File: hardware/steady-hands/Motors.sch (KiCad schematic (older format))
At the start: 6 parts

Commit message: Adds new components
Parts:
- removed Q?: VND5N07-E, Package_TO_SOT_SMD:TO-252-2, symbol Device:Q_NMOS_GDS
- removed R?: 0, symbol Device:R
- added Q?: DMN2004WKQ, Package_TO_SOT_SMD:SOT-323_SC-70, symbol Transistor_FET:DMN2041L
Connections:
- wire segments 20 -> 19
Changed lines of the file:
@@
 $Descr A4 11693 8268
 encoding utf-8
-Sheet 4 6
+Sheet 4 7
 Title ""
 Date ""
@@
 	1    6950 3700
 	1    0    0    -1
-$EndComp
-$Comp
-L Device:Q_NMOS_GDS Q?
-U 1 1 5EF9AE62
-P 5300 3650
-F 0 "Q?" H 5504 3696 50  0000 L CNN
-F 1 "VND5N07-E" H 5504 3605 50  0000 L CNN
-F 2 "Package_TO_SOT_SMD:TO-252-2" H 5500 3750 50  0001 C CNN
-F 3 "~" H 5300 3650 50  0001 C CNN
-	1    5300 3650
-	1    0    0    -1
-$EndComp
-$Comp
-L Device:R R?
-U 1 1 5EF9AE68
-P 4700 3650
-F 0 "R?" V 4493 3650 50  0000 C CNN
-F 1 "0" V 4584 3650 50  0000 C CNN
-F 2 "" V 4630 3650 50  0001 C CNN
-F 3 "~" H 4700 3650 50  0001 C CNN
-	1    4700 3650
-	0    1    1    0
 $EndComp
 $Comp
@@
 	5100 3650 5000 3650
 Wire Wire Line
-	4550 3650 4400 3650
-Wire Wire Line
 	5000 3800 5000 3650
 Connection ~ 5000 3650
-Wire Wire Line
-	5000 3650 4850 3650
 Wire Wire Line
 	5400 3850 5400 4300
@@
 Text HLabel 4400 3650 0    50   Input ~ 0
 EN
+Wire Wire Line
+	4400 3650 5000 3650
+$Comp
+L Transistor_FET:DMN2041L Q?
+U 1 1 5EFAB5CE
+P 5300 3650
+F 0 "Q?" H 5504 3696 50  0000 L CNN
+F 1 "DMN2004WKQ" H 5504 3605 50  0000 L CNN
+F 2 "Package_TO_SOT_SMD:SOT-323_SC-70" H 5500 3575 50  0001 L CIN
+F 3 "https://www.mouser.com/datasheet/2/115/DMN2004WKQ-1019748.pdf" H 5300 3650 50  0001 L CNN
+	1    5300 3650
+	1    0    0    -1
+$EndComp
 $EndSCHEMATC

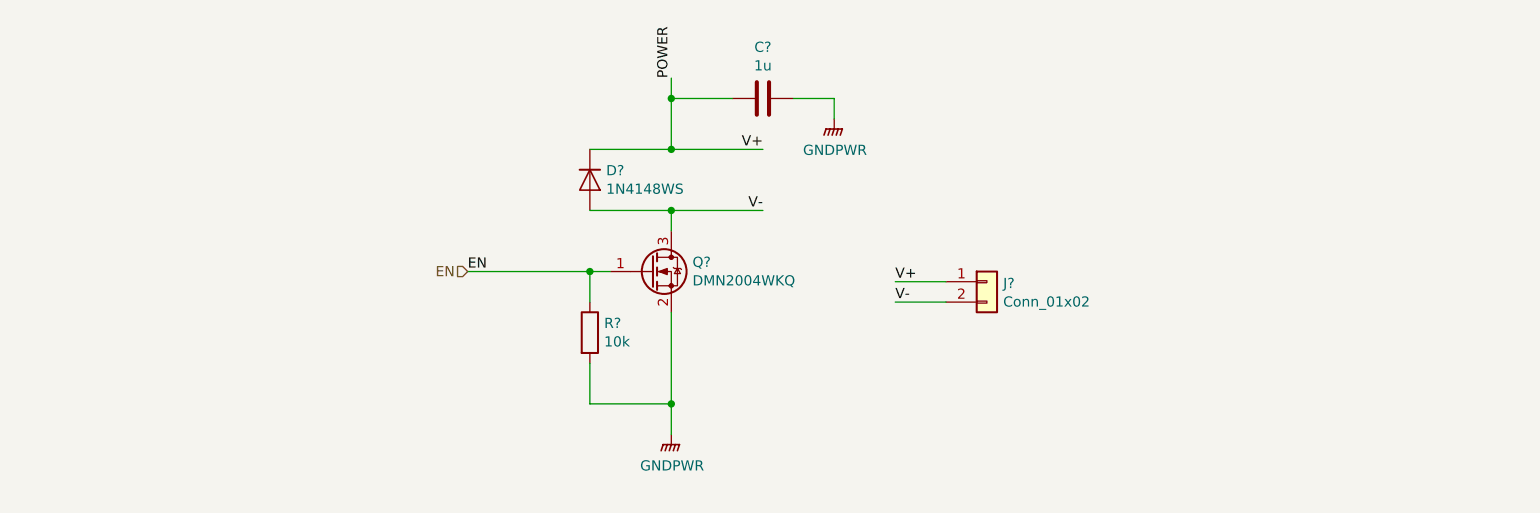
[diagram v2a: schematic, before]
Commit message: Adds second motor components
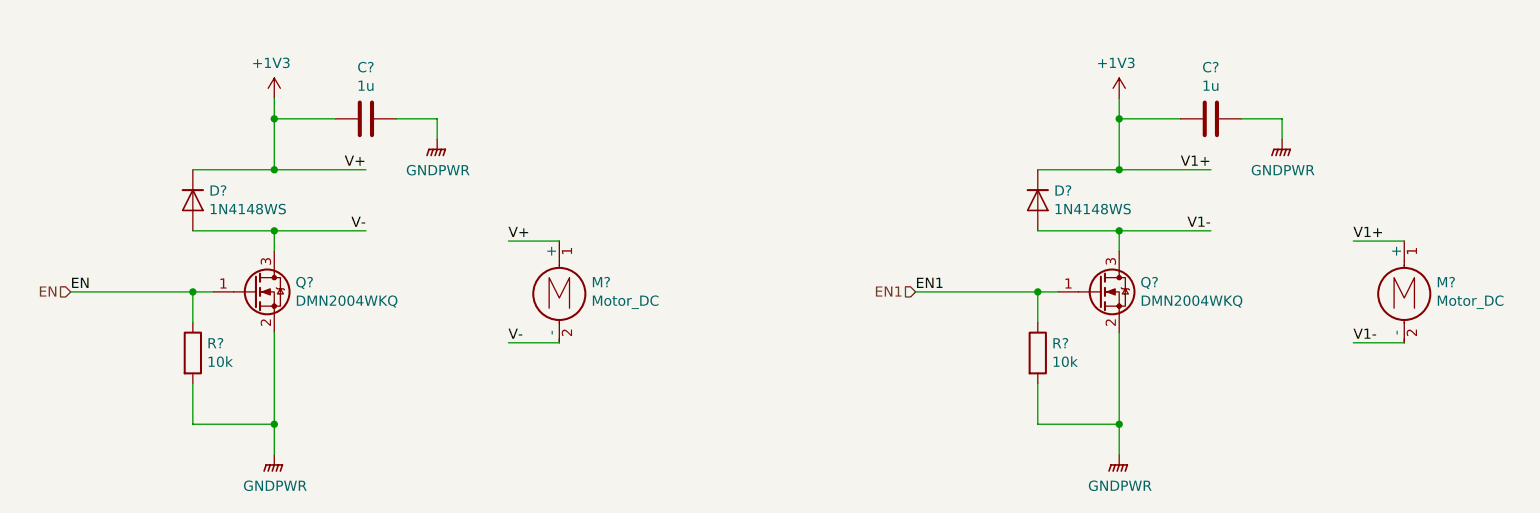
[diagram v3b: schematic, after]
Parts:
- removed J?: Conn_01x02, symbol Connector_Generic:Conn_01x02
- added C?: 1u, symbol Device:C
- added D?: 1N4148WS, Diode_SMD:D_SOD-323, symbol Diode:1N4148WS
- added M? (x2): Motor_DC, symbol Motor:Motor_DC
- added Q?: DMN2004WKQ, Package_TO_SOT_SMD:SOT-323_SC-70, symbol Transistor_FET:DMN2041L
- added R?: 10k, symbol Device:R
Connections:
- net GNDPWR: now also C?.1, Q?.2 (S), R?.2
- net V-: now also M?.2 (-)
- net POWER renamed +1V3
- net +1V3: now also C?.2, D?.1 (K), M?.1 (+), M?.1 (+)
- new net EN1: Q?.1 (G), R?.1
- new net V1-: D?.2 (A), M?.2 (-), Q?.3 (D)
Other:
- moved on the sheet: C?, D?, Q?, R?

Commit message: Completes schematic connections
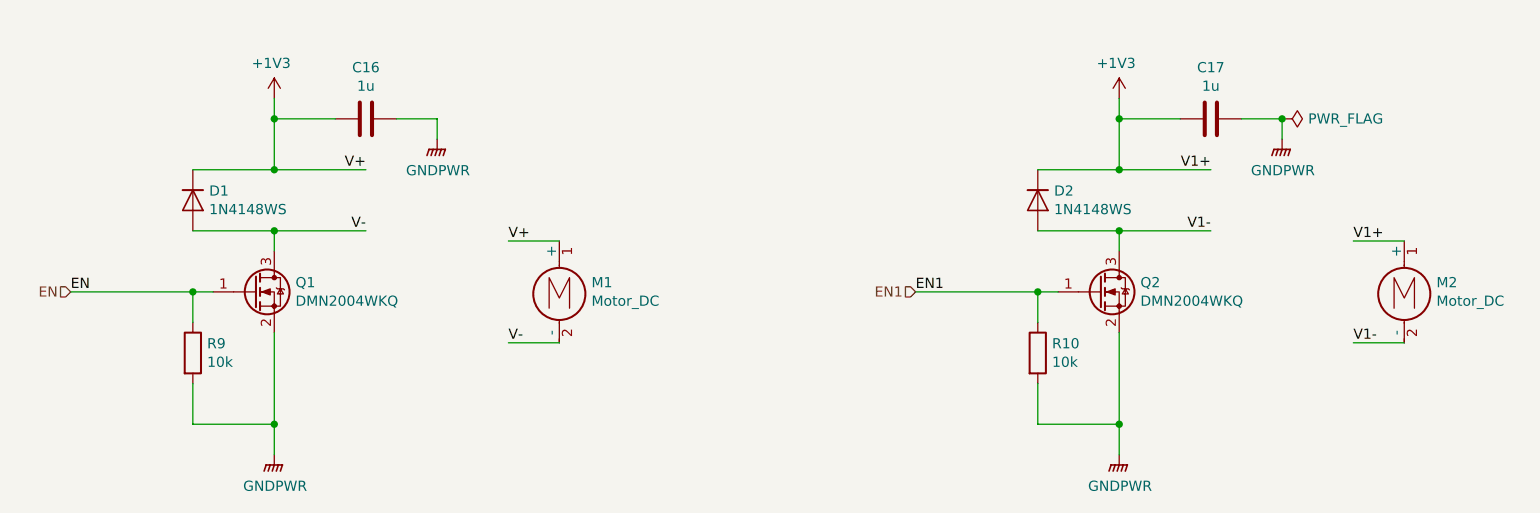
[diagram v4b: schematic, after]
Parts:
- gave numbers to parts that had none: 10
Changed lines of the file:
@@
 $Descr A4 11693 8268
 encoding utf-8
-Sheet 4 7
+Sheet 3 7
 Title ""
 Date ""
@@
 $EndDescr
 $Comp
-L Device:R R?
+L Device:R R9
 U 1 1 5EF9AE6E
 P 3050 4050
-F 0 "R?" H 3120 4096 50  0000 L CNN
+F 0 "R9" H 3120 4096 50  0000 L CNN
 F 1 "10k" H 3120 4005 50  0000 L CNN
 F 2 "" V 2980 4050 50  0001 C CNN
@@
 $EndComp
 $Comp
-L Diode:1N4148WS D?
+L Diode:1N4148WS D1
 U 1 1 5EF9AE74
 P 3050 3300
-F 0 "D?" V 3004 3380 50  0000 L CNN
+F 0 "D1" V 3004 3380 50  0000 L CNN
 F 1 "1N4148WS" V 3095 3380 50  0000 L CNN
 F 2 "Diode_SMD:D_SOD-323" H 3050 3125 50  0001 C CNN
@@
 $EndComp
 $Comp
-L Device:C C?
+L Device:C C16
 U 1 1 5EF9AE7A
 P 3900 2900
-F 0 "C?" V 3648 2900 50  0000 C CNN
+F 0 "C16" V 3648 2900 50  0000 C CNN
 F 1 "1u" V 3739 2900 50  0000 C CNN
 F 2 "" H 3938 2750 50  0001 C CNN
@@
 Connection ~ 3450 4400
 $Comp
-L power:GNDPWR #PWR?
+L power:GNDPWR #PWR0126
 U 1 1 5EF9AE97
 P 4250 3000
-F 0 "#PWR?" H 4250 2800 50  0001 C CNN
+F 0 "#PWR0126" H 4250 2800 50  0001 C CNN
 F 1 "GNDPWR" H 4254 2846 50  0000 C CNN
 F 2 "" H 4250 2950 50  0001 C CNN
@@
 $EndComp
 $Comp
-L power:GNDPWR #PWR?
+L power:GNDPWR #PWR0127
 U 1 1 5EF9AE9D
 P 3450 4550
-F 0 "#PWR?" H 3450 4350 50  0001 C CNN
+F 0 "#PWR0127" H 3450 4350 50  0001 C CNN
 F 1 "GNDPWR" H 3454 4396 50  0000 C CNN
 F 2 "" H 3450 4500 50  0001 C CNN
@@
 	2450 3750 3050 3750
 $Comp
-L Transistor_FET:DMN2041L Q?
+L Transistor_FET:DMN2041L Q1
 U 1 1 5EFAB5CE
 P 3350 3750
-F 0 "Q?" H 3554 3796 50  0000 L CNN
+F 0 "Q1" H 3554 3796 50  0000 L CNN
 F 1 "DMN2004WKQ" H 3554 3705 50  0000 L CNN
 F 2 "Package_TO_SOT_SMD:SOT-323_SC-70" H 3550 3675 50  0001 L CIN
@@
 $EndComp
 $Comp
-L Motor:Motor_DC M?
+L Motor:Motor_DC M1
 U 1 1 5F06BBCD
 P 4850 3700
-F 0 "M?" H 5008 3696 50  0000 L CNN
+F 0 "M1" H 5008 3696 50  0000 L CNN
 F 1 "Motor_DC" H 5008 3605 50  0000 L CNN
 F 2 "" H 4850 3610 50  0001 C CNN
@@
 $EndComp
 $Comp
-L Device:R R?
+L Device:R R10
 U 1 1 5F074CD3
 P 7200 4050
-F 0 "R?" H 7270 4096 50  0000 L CNN
+F 0 "R10" H 7270 4096 50  0000 L CNN
 F 1 "10k" H 7270 4005 50  0000 L CNN
 F 2 "" V 7130 4050 50  0001 C CNN
@@
 $EndComp
 $Comp
-L Diode:1N4148WS D?
+L Diode:1N4148WS D2
 U 1 1 5F074CD9
 P 7200 3300
-F 0 "D?" V 7154 3380 50  0000 L CNN
+F 0 "D2" V 7154 3380 50  0000 L CNN
 F 1 "1N4148WS" V 7245 3380 50  0000 L CNN
 F 2 "Diode_SMD:D_SOD-323" H 7200 3125 50  0001 C CNN
@@
 $EndComp
 $Comp
-L Device:C C?
+L Device:C C17
 U 1 1 5F074CDF
 P 8050 2900
-F 0 "C?" V 7798 2900 50  0000 C CNN
+F 0 "C17" V 7798 2900 50  0000 C CNN
 F 1 "1u" V 7889 2900 50  0000 C CNN
 F 2 "" H 8088 2750 50  0001 C CNN
@@
 Connection ~ 7600 4400
 $Comp
-L power:GNDPWR #PWR?
+L power:GNDPWR #PWR0128
 U 1 1 5F074CFA
 P 8400 3000
-F 0 "#PWR?" H 8400 2800 50  0001 C CNN
+F 0 "#PWR0128" H 8400 2800 50  0001 C CNN
 F 1 "GNDPWR" H 8404 2846 50  0000 C CNN
 F 2 "" H 8400 2950 50  0001 C CNN
@@
 $EndComp
 $Comp
-L power:GNDPWR #PWR?
+L power:GNDPWR #PWR0129
 U 1 1 5F074D00
 P 7600 4550
-F 0 "#PWR?" H 7600 4350 50  0001 C CNN
+F 0 "#PWR0129" H 7600 4350 50  0001 C CNN
 F 1 "GNDPWR" H 7604 4396 50  0000 C CNN
 F 2 "" H 7600 4500 50  0001 C CNN
@@
 	6600 3750 7200 3750
 $Comp
-L Transistor_FET:DMN2041L Q?
+L Transistor_FET:DMN2041L Q2
 U 1 1 5F074D10
 P 7500 3750
-F 0 "Q?" H 7704 3796 50  0000 L CNN
+F 0 "Q2" H 7704 3796 50  0000 L CNN
 F 1 "DMN2004WKQ" H 7704 3705 50  0000 L CNN
 F 2 "Package_TO_SOT_SMD:SOT-323_SC-70" H 7700 3675 50  0001 L CIN
@@
 $EndComp
 $Comp
-L Motor:Motor_DC M?
+L Motor:Motor_DC M2
 U 1 1 5F074D16
 P 9000 3700
-F 0 "M?" H 9158 3696 50  0000 L CNN
+F 0 "M2" H 9158 3696 50  0000 L CNN
 F 1 "Motor_DC" H 9158 3605 50  0000 L CNN
 F 2 "" H 9000 3610 50  0001 C CNN
@@
 $EndComp
 $Comp
-L steady-hands:+1V3 #PWR?
+L steady-hands:+1V3 #PWR0130
 U 1 1 5F075388
 P 3450 2850
-F 0 "#PWR?" H 3550 2850 50  0001 C CNN
+F 0 "#PWR0130" H 3550 2850 50  0001 C CNN
 F 1 "+1V3" H 3435 3073 50  0000 C CNN
 F 2 "" H 3450 2850 50  0001 C CNN
@@
 $EndComp
 $Comp
-L steady-hands:+1V3 #PWR?
+L steady-hands:+1V3 #PWR0131
 U 1 1 5F0783A4
 P 7600 2850
-F 0 "#PWR?" H 7700 2850 50  0001 C CNN
+F 0 "#PWR0131" H 7700 2850 50  0001 C CNN
 F 1 "+1V3" H 7585 3073 50  0000 C CNN
 F 2 "" H 7600 2850 50  0001 C CNN
@@
 	1    0    0    -1
 $EndComp
+$Comp
+L power:PWR_FLAG #FLG0107
+U 1 1 5F25484B
+P 8400 2900
+F 0 "#FLG0107" H 8400 2975 50  0001 C CNN
+F 1 "PWR_FLAG" V 8400 3028 50  0000 L CNN
+F 2 "" H 8400 2900 50  0001 C CNN
+F 3 "~" H 8400 2900 50  0001 C CNN
+	1    8400 2900
+	0    1    1    0
+$EndComp
+Connection ~ 8400 2900
 $EndSCHEMATC

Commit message: Edits label names and switch configuration
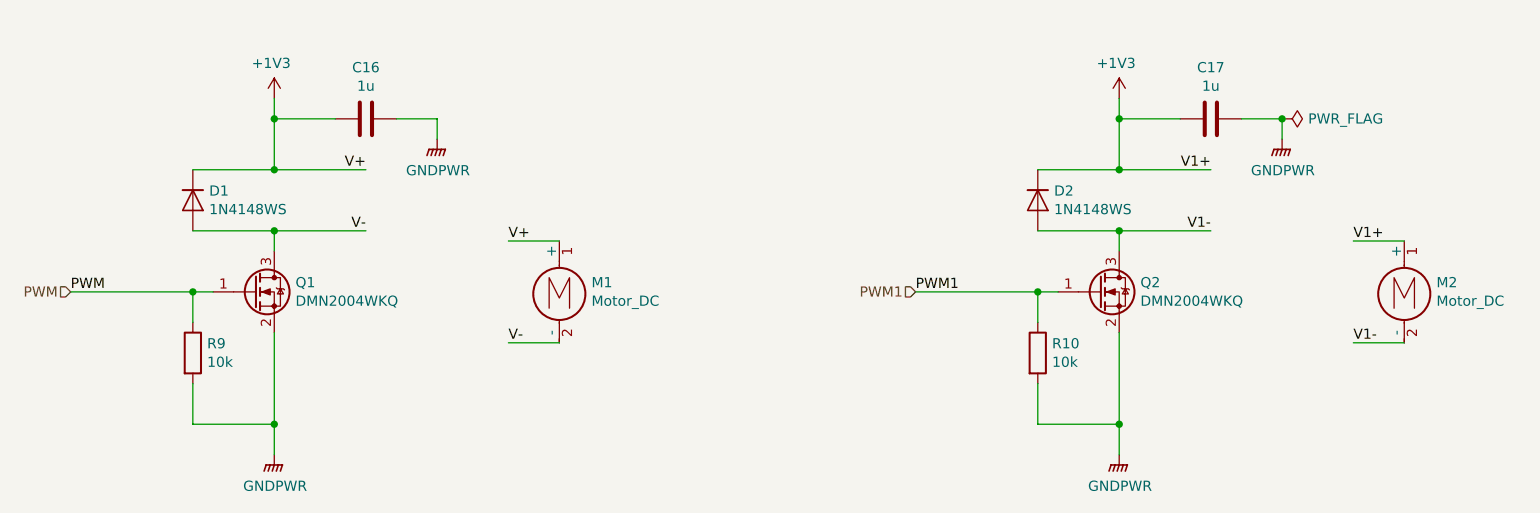
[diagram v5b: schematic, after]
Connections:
- net EN renamed PWM
- net EN1 renamed PWM1
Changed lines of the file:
@@
 V-
 Text Label 2450 3750 0    50   ~ 0
-EN
+PWM
 Text Label 4600 3500 0    50   ~ 0
 V+
@@
 	4850 4000 4600 4000
 Text HLabel 2450 3750 0    50   Input ~ 0
-EN
+PWM
 Wire Wire Line
 	2450 3750 3050 3750
@@
 V1-
 Text Label 6600 3750 0    50   ~ 0
-EN1
+PWM1
 Text Label 8750 3500 0    50   ~ 0
 V1+
@@
 	9000 4000 8750 4000
 Text HLabel 6600 3750 0    50   Input ~ 0
-EN1
+PWM1
 Wire Wire Line
 	6600 3750 7200 3750

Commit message: Adds footprints
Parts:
- C16, C17: footprint (none) -> Capacitor_SMD:C_0402_1005Metric
- R10, R9: footprint (none) -> Resistor_SMD:R_0402_1005Metric
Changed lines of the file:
@@
 $Descr A4 11693 8268
 encoding utf-8
-Sheet 3 7
+Sheet 2 6
 Title ""
 Date ""
@@
 F 0 "R9" H 3120 4096 50  0000 L CNN
 F 1 "10k" H 3120 4005 50  0000 L CNN
-F 2 "" V 2980 4050 50  0001 C CNN
+F 2 "Resistor_SMD:R_0402_1005Metric" V 2980 4050 50  0001 C CNN
 F 3 "~" H 3050 4050 50  0001 C CNN
 	1    3050 4050
@@
 F 0 "C16" V 3648 2900 50  0000 C CNN
 F 1 "1u" V 3739 2900 50  0000 C CNN
-F 2 "" H 3938 2750 50  0001 C CNN
+F 2 "Capacitor_SMD:C_0402_1005Metric" H 3938 2750 50  0001 C CNN
 F 3 "~" H 3900 2900 50  0001 C CNN
 	1    3900 2900
@@
 F 0 "R10" H 7270 4096 50  0000 L CNN
 F 1 "10k" H 7270 4005 50  0000 L CNN
-F 2 "" V 7130 4050 50  0001 C CNN
+F 2 "Resistor_SMD:R_0402_1005Metric" V 7130 4050 50  0001 C CNN
 F 3 "~" H 7200 4050 50  0001 C CNN
 	1    7200 4050
@@
 F 0 "C17" V 7798 2900 50  0000 C CNN
 F 1 "1u" V 7889 2900 50  0000 C CNN
-F 2 "" H 8088 2750 50  0001 C CNN
+F 2 "Capacitor_SMD:C_0402_1005Metric" H 8088 2750 50  0001 C CNN
 F 3 "~" H 8050 2900 50  0001 C CNN
 	1    8050 2900
@@
 Connection ~ 8400 2900
 $Comp
-L steady-hands:+1V3 #PWR?
+L steady-hands:+1V3 #PWR0130
 U 1 1 5F0DECEF
 P 3450 2850
-F 0 "#PWR?" H 3550 2850 50  0001 C CNN
+F 0 "#PWR0130" H 3550 2850 50  0001 C CNN
 F 1 "+1V3" H 3435 3073 50  0000 C CNN
 F 2 "" H 3450 2850 50  0001 C CNN
@@
 $EndComp
 $Comp
-L steady-hands:+1V3 #PWR?
+L steady-hands:+1V3 #PWR0131
 U 1 1 5F0DF498
 P 7600 2850
-F 0 "#PWR?" H 7700 2850 50  0001 C CNN
+F 0 "#PWR0131" H 7700 2850 50  0001 C CNN
 F 1 "+1V3" H 7585 3073 50  0000 C CNN
 F 2 "" H 7600 2850 50  0001 C CNN

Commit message: Adds all footprints to board
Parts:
- M1, M2: footprint (none) -> Sij_Motors:316040005
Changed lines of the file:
@@
 F 0 "M1" H 5008 3696 50  0000 L CNN
 F 1 "Motor_DC" H 5008 3605 50  0000 L CNN
-F 2 "" H 4850 3610 50  0001 C CNN
+F 2 "Sij_Motors:316040005" H 4850 3610 50  0001 C CNN
 F 3 "~" H 4850 3610 50  0001 C CNN
 	1    4850 3700
@@
 F 0 "M2" H 9158 3696 50  0000 L CNN
 F 1 "Motor_DC" H 9158 3605 50  0000 L CNN
-F 2 "" H 9000 3610 50  0001 C CNN
+F 2 "Sij_Motors:316040005" H 9000 3610 50  0001 C CNN
 F 3 "~" H 9000 3610 50  0001 C CNN
 	1    9000 3700
